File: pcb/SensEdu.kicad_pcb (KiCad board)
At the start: 4 copper layers, 92.7 x 53.4 mm, 139 parts, among them IC1 ADA4511-2ARMZ, IC2 SHT35-DIS-B2.5KS, J1 Analog, J10 Conn_01x04_Pin, J11 Conn_01x04_Pin, J2 Analog, J3 Power, J4 Digital, J5 PWM, J6 PWM, J7 Communication, J8 Conn_01x04_Pin, J9 Conn_01x04_Pin, SW2 NC7SB3157P6X, U1 LM27762DSST, U10 DPS368XTSA1, U2 NCP1117-2.5_SOT223, U3 LT1790ACS6-1.25, U4 AD8426ACPZ-R7, U5 AD8426ACPZ-R7, U6 AD8426ACPZ-R7, U7 AD8426ACPZ-R7, U8 NC7SB3157P6X

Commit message: in works
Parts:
- moved TP_3V3 0.36 mm to (109.0, 66.6)
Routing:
- net +3.3V: track 277.4 -> 267.5 mm, vias 13 -> 14
- net +1.25V_REF: track 80.2 -> 87.9 mm
- net -3V3: track 58.3 -> 59.3 mm
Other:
- board text added: "OP1"
- board text added: "OP2"
- board text added: "OP3"
- board text removed: "AMP1"
- board text removed: "AMP2"
- board text removed: "AMP3"
- board text removed: "AMP4"

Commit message: fix: PCB final fixes
Added simulation for dc offset after ac coupling
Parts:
- removed TP_3V3: TestPoint, TestPoint:TestPoint_THTPad_D2.0mm_Drill1.0mm
- added C52: 1u, Capacitor_SMD:C_0805_2012Metric, F.Cu at (148.0, 67.4)
- added C55: 1u, Capacitor_SMD:C_0805_2012Metric, F.Cu at (156.8, 80.8)
- added TP_TX1: TestPoint, TestPoint:TestPoint_THTPad_D2.0mm_Drill1.0mm, F.Cu at (159.5, 82.3)
- C50, C51: value 2.2u -> 100n
- R30, R31: value 22k -> 1.2k
- moved TP_1V25 0.70 mm to (160.1, 85.9)
- renumbered C52 to C53, C53 to C54, C54 to C56, C55 to C57, C56 to C58, C57 to C59, MIC2 to MK2, MIC3 to MK3, MIC4 to MK4, SW2 to U9
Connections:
- C6 pad 1: +3.3V -> /3V3_INO
- C7 pad 1: +3.3V -> /3V3_INO
- J3 pad 4: /3V3 -> /3V3_INO
- U2 pad 3: +3.3V -> /3V3_INO
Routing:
- net /3V3_INO: track 0.00 -> 77.3 mm
- net +3.3V: track 267.5 -> 246.7 mm
- net /Speakers/+IN_CH1: track 9.82 -> 15.7 mm
- net /+5V_ARDUINO: track 68.0 -> 72.1 mm
- net GND: track 116.6 -> 120.0 mm, vias 86 -> 88
- net +1.25V_REF: track 87.9 -> 85.3 mm
- net -3V3: track 59.3 -> 60.2 mm
- net /OUT_MIC1: track 59.8 -> 60.0 mm, vias 3 -> 5
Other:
- board text removed: "3.3V->1.25V"

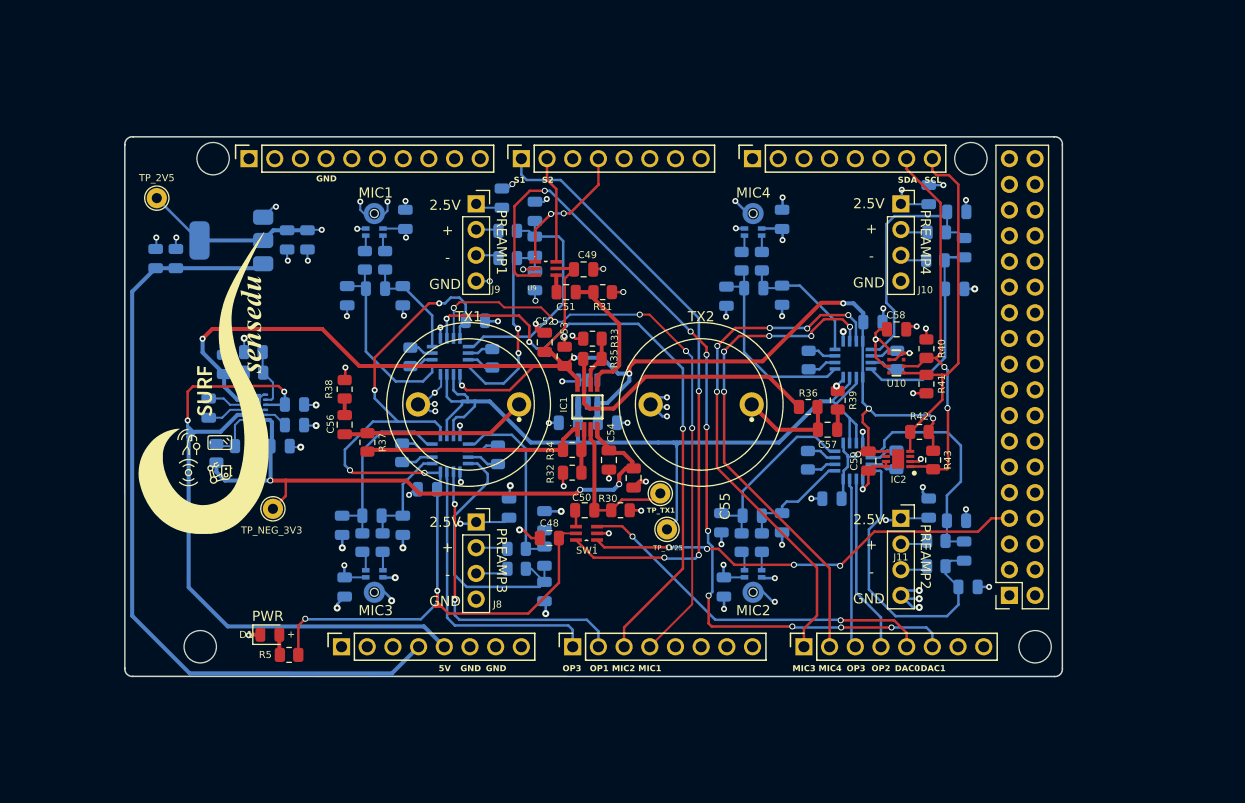
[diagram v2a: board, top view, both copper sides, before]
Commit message: feat: Redraw PCB layout
- Change supply polarity and pin numbers of ADA4511
- Change cap of switches to 100n to reduce bom
- Change supply of sensors to unison 3.3V
- Rearrange mic and amps pins
- Add mountains
- Add Infineon logo
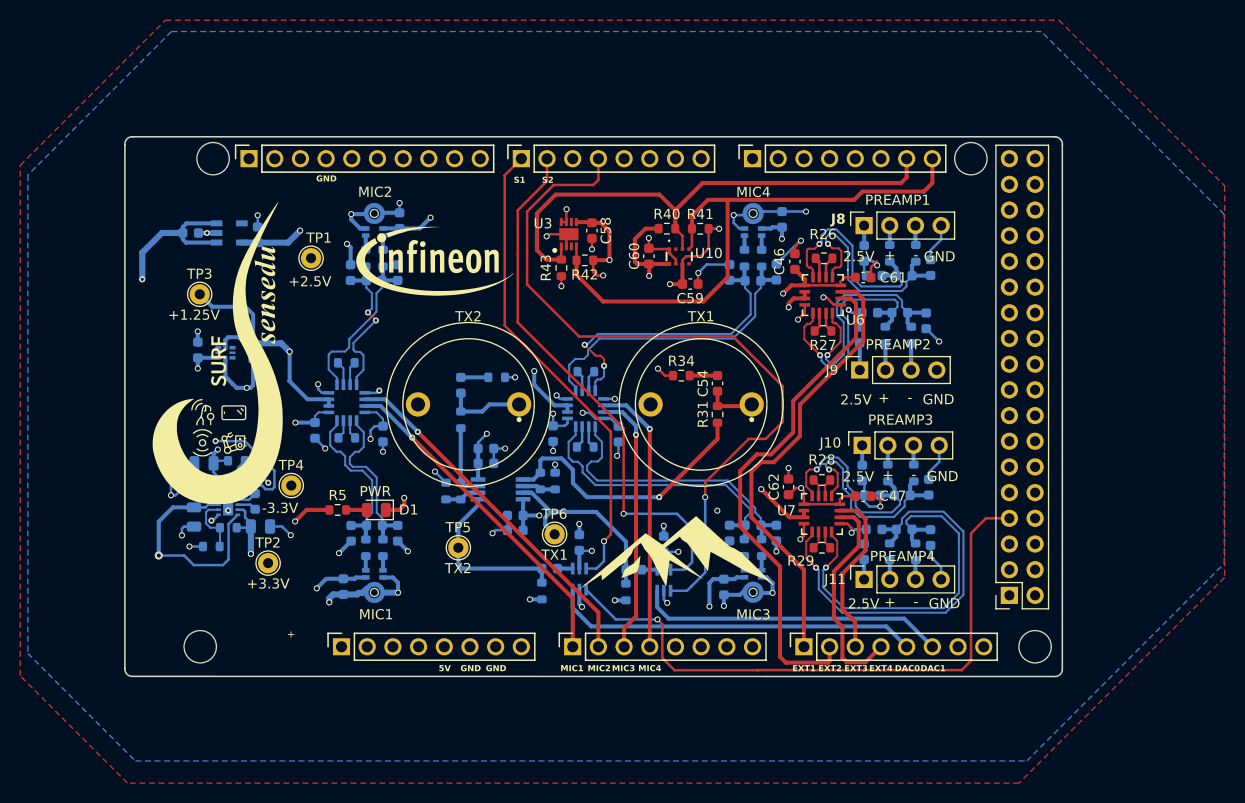
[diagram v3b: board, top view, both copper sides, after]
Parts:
- removed the C34 at (144.5, 83.8)
- removed the C46 at (188.8, 85.0)
- removed the C47 at (186.0, 83.8)
- removed the C6 at (111.6, 59.1)
- removed the C9 at (124.6, 57.2)
- removed IC2: SHT35-DIS-B2.5KS, SensEdu:SHT35-DIS-B2.5KS
- removed the R20 at (145.3, 87.8)
- removed the R26 at (186.7, 59.2)
- removed the R27 at (186.8, 56.5)
- removed the R28 at (186.8, 89.5)
- removed the R29 at (186.8, 87.0)
- removed TP_1V25, TP_2V5, TP_NEG_3V3, TP_TX1: TestPoint, TestPoint:TestPoint_THTPad_D2.0mm_Drill1.0mm
- removed the U2 at (117.0, 57.3)
- added C1: 1u, Capacitor_SMD:C_0603_1608Metric, B.Cu at (132.0, 76.4)
- added C3: 1u, Capacitor_SMD:C_0603_1608Metric, B.Cu at (155.3, 76.4)
- added C35: 470p, Capacitor_SMD:C_0603_1608Metric, B.Cu at (183.6, 85.9)
- added C36: 470p, Capacitor_SMD:C_0603_1608Metric, B.Cu at (183.4, 82.5)
- added C37: 470p, Capacitor_SMD:C_0603_1608Metric, B.Cu at (183.6, 60.8)
- added C59: 100n, Capacitor_SMD:C_0603_1608Metric, F.Cu at (162.4, 61.6)
- added C61: 1u, Capacitor_SMD:C_0603_1608Metric, F.Cu at (179.5, 61.0)
- added C62: 1u, Capacitor_SMD:C_0603_1608Metric, F.Cu at (172.1, 81.7)
- added G***: LOGO, LOGO, F.Cu at (137.4, 59.4)
- added G***: LOGO, LOGO, F.Cu at (161.1, 87.9)
- added R18: 3.9k, Resistor_SMD:R_0603_1608Metric, B.Cu at (184.7, 58.6)
- added R22: 3.9k, Resistor_SMD:R_0603_1608Metric, B.Cu at (184.5, 80.3)
- added R23: 3.9k, Resistor_SMD:R_0603_1608Metric, B.Cu at (182.0, 80.3)
- added R24: 3.9k, Resistor_SMD:R_0603_1608Metric, B.Cu at (184.7, 88.1)
- added R25: 3.9k, Resistor_SMD:R_0603_1608Metric, B.Cu at (182.1, 88.1)
- added TP1: +2.5V, TestPoint:TestPoint_THTPad_D2.0mm_Drill1.0mm, F.Cu at (124.9, 59.0)
- added TP2: +3.3V, TestPoint:TestPoint_THTPad_D2.0mm_Drill1.0mm, F.Cu at (120.7, 89.2)
- added TP3: +1.25V, TestPoint:TestPoint_THTPad_D2.0mm_Drill1.0mm, F.Cu at (113.9, 62.6)
- added TP4: -3.3V, TestPoint:TestPoint_THTPad_D2.0mm_Drill1.0mm, F.Cu at (123.0, 81.5)
- added TP5: TX2, TestPoint:TestPoint_THTPad_D2.0mm_Drill1.0mm, F.Cu at (139.5, 87.7)
- added TP6: TX1, TestPoint:TestPoint_THTPad_D2.0mm_Drill1.0mm, F.Cu at (149.0, 86.3)
- added U1: LDLN025M25R, SamacSys_Parts:SOT95P280X145-5N, B.Cu at (116.8, 56.5)
- added U13: TS3312AQPR, SamacSys_Parts:TS3312AQPR, B.Cu at (116.5, 68.4)
- C10: renamed from C8; value 100n -> 1u; footprint Capacitor_SMD:C_0805_2012Metric -> Capacitor_SMD:C_0603_1608Metric
- C11, C14, C17, C40, C42, C44: footprint Capacitor_SMD:C_0805_2012Metric -> Capacitor_SMD:C_0603_1608Metric
- C12: renamed from C25; footprint Capacitor_SMD:C_0805_2012Metric -> Capacitor_SMD:C_0603_1608Metric
- C13: renamed from C20; footprint Capacitor_SMD:C_0805_2012Metric -> Capacitor_SMD:C_0603_1608Metric
- C15: renamed from C26; footprint Capacitor_SMD:C_0805_2012Metric -> Capacitor_SMD:C_0603_1608Metric
- C16: renamed from C13; footprint Capacitor_SMD:C_0805_2012Metric -> Capacitor_SMD:C_0603_1608Metric
- C18: renamed from C23; footprint Capacitor_SMD:C_0805_2012Metric -> Capacitor_SMD:C_0603_1608Metric
- C19: renamed from C28; footprint Capacitor_SMD:C_0805_2012Metric -> Capacitor_SMD:C_0603_1608Metric
- C2: renamed from C7; value 100n -> 1u; footprint Capacitor_SMD:C_0805_2012Metric -> Capacitor_SMD:C_0603_1608Metric
- C20: renamed from C15; footprint Capacitor_SMD:C_0805_2012Metric -> Capacitor_SMD:C_0603_1608Metric
- C21: renamed from C24; footprint Capacitor_SMD:C_0805_2012Metric -> Capacitor_SMD:C_0603_1608Metric
- C22: renamed from C18; footprint Capacitor_SMD:C_0805_2012Metric -> Capacitor_SMD:C_0603_1608Metric
- C23: renamed from C27; footprint Capacitor_SMD:C_0805_2012Metric -> Capacitor_SMD:C_0603_1608Metric
- C24: renamed from C16; footprint Capacitor_SMD:C_0805_2012Metric -> Capacitor_SMD:C_0603_1608Metric
- C25: renamed from C19; footprint Capacitor_SMD:C_0805_2012Metric -> Capacitor_SMD:C_0603_1608Metric
- C26: renamed from C22; footprint Capacitor_SMD:C_0805_2012Metric -> Capacitor_SMD:C_0603_1608Metric
- C27: renamed from C29; footprint Capacitor_SMD:C_0805_2012Metric -> Capacitor_SMD:C_0603_1608Metric
- C28: renamed from C21; footprint Capacitor_SMD:C_0805_2012Metric -> Capacitor_SMD:C_0603_1608Metric
- C29: renamed from C12; footprint Capacitor_SMD:C_0805_2012Metric -> Capacitor_SMD:C_0603_1608Metric
- C30, C33: value 100p -> 100n; footprint Capacitor_SMD:C_0805_2012Metric -> Capacitor_SMD:C_0603_1608Metric
- C31: renamed from C39; footprint Capacitor_SMD:C_0805_2012Metric -> Capacitor_SMD:C_0603_1608Metric
- C32: value 470p -> 100n; footprint Capacitor_SMD:C_0805_2012Metric -> Capacitor_SMD:C_0603_1608Metric
- C34: renamed from C37; footprint Capacitor_SMD:C_0805_2012Metric -> Capacitor_SMD:C_0603_1608Metric
- C38: renamed from C35; footprint Capacitor_SMD:C_0805_2012Metric -> Capacitor_SMD:C_0603_1608Metric
- C39: renamed from C38; footprint Capacitor_SMD:C_0805_2012Metric -> Capacitor_SMD:C_0603_1608Metric
- C4: renamed from C10; value 100n -> 1u; footprint Capacitor_SMD:C_0805_2012Metric -> Capacitor_SMD:C_0603_1608Metric
- C41, C45: value 470p -> 100p; footprint Capacitor_SMD:C_0805_2012Metric -> Capacitor_SMD:C_0603_1608Metric
- C43: value 100n -> 100p; footprint Capacitor_SMD:C_0805_2012Metric -> Capacitor_SMD:C_0603_1608Metric
- C46: renamed from C31; footprint Capacitor_SMD:C_0805_2012Metric -> Capacitor_SMD:C_0603_1608Metric; moved to F.Cu
- C47: renamed from C36; footprint Capacitor_SMD:C_0805_2012Metric -> Capacitor_SMD:C_0603_1608Metric; moved to F.Cu
- C48: value 10n -> 100n; footprint Capacitor_SMD:C_0805_2012Metric -> Capacitor_SMD:C_0603_1608Metric; moved to B.Cu
- C49: renamed from C52; footprint Capacitor_SMD:C_0805_2012Metric -> Capacitor_SMD:C_0603_1608Metric; moved to B.Cu
- C50: renamed from C53; footprint Capacitor_SMD:C_0805_2012Metric -> Capacitor_SMD:C_0603_1608Metric; moved to B.Cu
- C51: renamed from C54; footprint Capacitor_SMD:C_0805_2012Metric -> Capacitor_SMD:C_0603_1608Metric; moved to B.Cu
- C52: renamed from C55; footprint Capacitor_SMD:C_0805_2012Metric -> Capacitor_SMD:C_0603_1608Metric; moved to B.Cu
- C53: renamed from C50; footprint Capacitor_SMD:C_0805_2012Metric -> Capacitor_SMD:C_0603_1608Metric; moved to B.Cu
- C54: renamed from C56; footprint Capacitor_SMD:C_0805_2012Metric -> Capacitor_SMD:C_0603_1608Metric
- C55: renamed from C57; footprint Capacitor_SMD:C_0805_2012Metric -> Capacitor_SMD:C_0603_1608Metric; moved to B.Cu
- C56: renamed from C49; value 10n -> 100n; footprint Capacitor_SMD:C_0805_2012Metric -> Capacitor_SMD:C_0603_1608Metric; moved to B.Cu
- C57: renamed from C51; footprint Capacitor_SMD:C_0805_2012Metric -> Capacitor_SMD:C_0603_1608Metric; moved to B.Cu
- C58: renamed from C59; footprint Capacitor_SMD:C_0805_2012Metric -> Capacitor_SMD:C_0603_1608Metric
- C60: renamed from C58; footprint Capacitor_SMD:C_0805_2012Metric -> Capacitor_SMD:C_0603_1608Metric
- C8: renamed from C2; footprint Capacitor_SMD:C_0805_2012Metric -> Capacitor_SMD:C_0603_1608Metric
- R1, R17, R19, R2, R3, R4, R42, R43, R5: footprint Resistor_SMD:R_0805_2012Metric -> Resistor_SMD:R_0603_1608Metric
- R10: renamed from R8; footprint Resistor_SMD:R_0805_2012Metric -> Resistor_SMD:R_0603_1608Metric
- R11: renamed from R10; footprint Resistor_SMD:R_0805_2012Metric -> Resistor_SMD:R_0603_1608Metric
- R12: renamed from R13; footprint Resistor_SMD:R_0805_2012Metric -> Resistor_SMD:R_0603_1608Metric
- R13: renamed from R16; footprint Resistor_SMD:R_0805_2012Metric -> Resistor_SMD:R_0603_1608Metric
- R14: renamed from R6; footprint Resistor_SMD:R_0805_2012Metric -> Resistor_SMD:R_0603_1608Metric
- R15: renamed from R11; footprint Resistor_SMD:R_0805_2012Metric -> Resistor_SMD:R_0603_1608Metric
- R16: renamed from R12; footprint Resistor_SMD:R_0805_2012Metric -> Resistor_SMD:R_0603_1608Metric
- R20: renamed from R22; footprint Resistor_SMD:R_0805_2012Metric -> Resistor_SMD:R_0603_1608Metric
- R21: renamed from R24; footprint Resistor_SMD:R_0805_2012Metric -> Resistor_SMD:R_0603_1608Metric
- R26: renamed from R18; footprint Resistor_SMD:R_0805_2012Metric -> Resistor_SMD:R_0603_1608Metric; moved to F.Cu
- R27: renamed from R21; footprint Resistor_SMD:R_0805_2012Metric -> Resistor_SMD:R_0603_1608Metric; moved to F.Cu
- R28: renamed from R23; footprint Resistor_SMD:R_0805_2012Metric -> Resistor_SMD:R_0603_1608Metric; moved to F.Cu
- R29: renamed from R25; footprint Resistor_SMD:R_0805_2012Metric -> Resistor_SMD:R_0603_1608Metric; moved to F.Cu
- R30, R32: footprint Resistor_SMD:R_0805_2012Metric -> Resistor_SMD:R_0603_1608Metric; moved to B.Cu
- R31: renamed from R37; footprint Resistor_SMD:R_0805_2012Metric -> Resistor_SMD:R_0603_1608Metric
- R33: renamed from R34; footprint Resistor_SMD:R_0805_2012Metric -> Resistor_SMD:R_0603_1608Metric; moved to B.Cu
- R34: renamed from R38; footprint Resistor_SMD:R_0805_2012Metric -> Resistor_SMD:R_0603_1608Metric
- R35: renamed from R36; footprint Resistor_SMD:R_0805_2012Metric -> Resistor_SMD:R_0603_1608Metric; moved to B.Cu
- R36: renamed from R33; footprint Resistor_SMD:R_0805_2012Metric -> Resistor_SMD:R_0603_1608Metric; moved to B.Cu
- R37: renamed from R39; footprint Resistor_SMD:R_0805_2012Metric -> Resistor_SMD:R_0603_1608Metric; moved to B.Cu
- R38: renamed from R35; footprint Resistor_SMD:R_0805_2012Metric -> Resistor_SMD:R_0603_1608Metric; moved to B.Cu
- R39: renamed from R31; footprint Resistor_SMD:R_0805_2012Metric -> Resistor_SMD:R_0603_1608Metric; moved to B.Cu
- R40, R41: value 5k6 -> 10k; footprint Resistor_SMD:R_0805_2012Metric -> Resistor_SMD:R_0603_1608Metric
- R6: renamed from R7; footprint Resistor_SMD:R_0805_2012Metric -> Resistor_SMD:R_0603_1608Metric
- R7: renamed from R9; footprint Resistor_SMD:R_0805_2012Metric -> Resistor_SMD:R_0603_1608Metric
- R8: renamed from R14; footprint Resistor_SMD:R_0805_2012Metric -> Resistor_SMD:R_0603_1608Metric
- R9: renamed from R15; footprint Resistor_SMD:R_0805_2012Metric -> Resistor_SMD:R_0603_1608Metric
- U11: renamed from IC1; footprint SensEdu:ADA4511 -> SamacSys_Parts:SOP65P490X110-8N; moved to B.Cu
- U3: value LT1790ACS6-1.25 -> SHT35-DIS-B2.5KS; footprint Package_TO_SOT_SMD:TSOT-23-6 -> SensEdu:SHT35-DIS-B2.5KS; moved to F.Cu
- U6, U7: moved to F.Cu
- U8, U9: moved to B.Cu
- moved R19 48.3 mm to (182.2, 58.6), turned to -90 degrees
- moved J8 48.3 mm to (179.6, 55.8), turned to 90 degrees
- moved C30 46.0 mm to (179.6, 58.6), turned to -90 degrees
- moved R26 45.9 mm to (175.7, 59.0), turned to 180 degrees
- moved C46 42.7 mm to (172.8, 59.4), turned to 90 degrees
- moved R43 41.4 mm to (149.7, 60.0), turned to 90 degrees
- moved J9 41.3 mm to (179.2, 70.1), turned to 90 degrees
- moved C10 41.1 mm to (113.7, 68.1), turned to 90 degrees
- moved R20 40.6 mm to (184.3, 66.6), turned to 90 degrees
- moved U6 40.0 mm to (175.5, 62.7), turned to -90 degrees
- moved C38 38.9 mm to (185.8, 65.2)
- moved R21 38.7 mm to (181.7, 66.6), turned to 90 degrees
- moved C31 37.9 mm to (179.2, 66.6)
- moved R42 37.2 mm to (152.0, 59.2)
- moved C54 37.1 mm to (165.1, 71.4)
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- renumbered C1 to C6, C3 to C7, C4 to C9, J3 to J1, J5 to J2, J1 to J3, J6 to J4, J2 to J5, J7 to J6, J4 to J7, MK3 to MK2, MK2 to MK3, TX2 to TX1, TX1 to TX2, U1 to U2
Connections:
- net /OUT_MIC7 renamed /AMP3_OUT
- net /OUT_MIC8 renamed /AMP4_OUT
- C14 pad 1: mic1_out1 -> mic1_out_P
- C14 pad 2: mic1_out2 -> mic1_out_N
- C15 pad 1: mic3_out1 -> mic2_out_P
- C15 pad 2: mic3_out2 -> mic2_out_N
- C16 pad 2: mic1_out2 -> mic1_out_N
- C17 pad 2: mic1_out1 -> mic1_out_P
- C18 pad 2: mic3_out2 -> mic2_out_N
- C19 pad 2: mic3_out1 -> mic2_out_P
- C22 pad 1: mic2_out1 -> mic3_out_P
- C22 pad 2: mic2_out2 -> mic3_out_N
- C23 pad 1: mic4_out1 -> mic4_out_P
- C23 pad 2: mic4_out2 -> mic4_out_N
- C24 pad 2: mic2_out2 -> mic3_out_N
- C25 pad 2: mic2_out1 -> mic3_out_P
- C26 pad 2: mic4_out2 -> mic4_out_N
- C27 pad 2: mic4_out1 -> mic4_out_P
- C30 pad 1: GND -> +2.5V
- C30 pad 2: mic5_out2 -> GND
- C32 pad 1: mic5_out1 -> +2.5V
- C32 pad 2: mic5_out2 -> GND
- C33 pad 1: GND -> +2.5V
- C33 pad 2: mic5_out1 -> GND
- C34 pad 1: mic6_out1 -> amp2_out_P
- C34 pad 2: mic6_out2 -> amp2_out_N
- C38 pad 2: mic6_out2 -> amp2_out_N
- C39 pad 2: mic6_out1 -> amp2_out_P
- C40 pad 2: mic7_out2 -> amp4_out_N
- C41 pad 1: mic7_out1 -> GND
- C41 pad 2: mic7_out2 -> amp4_out_P
- C42 pad 2: mic7_out1 -> amp3_out_N
- C43 pad 1: +2.5V -> GND
- C43 pad 2: GND -> amp3_out_P
- C44 pad 2: mic8_out2 -> amp1_out_N
- C45 pad 1: mic8_out1 -> GND
- C45 pad 2: mic8_out2 -> amp1_out_P
- C49 pad 1: +3.3V -> -3V3
- C50 pad 1: +3.3V -> -3V3
- C51 pad 2: -3V3 -> +3.3V
- C52 pad 1: -3V3 -> +3.3V
- C60 pad 1: +2.5V -> +3.3V
- J3 pad 1: /OUT_MIC5 -> /MIC1_OUT
- J3 pad 2: /OUT_MIC6 -> /MIC2_OUT
- J3 pad 3: /OUT_MIC2 -> /MIC3_OUT
- J3 pad 4: /OUT_MIC1 -> /MIC4_OUT
- J4 pad 1: S1 -> S2
- J4 pad 2: S2 -> S1
- J5 pad 1: /OUT_MIC3 -> /AMP1_OUT
- J5 pad 2: /OUT_MIC4 -> /AMP2_OUT
- R10 pad 2: mic2_out2 -> mic3_out_N
- R11 pad 2: mic2_out1 -> mic3_out_P
- R12 pad 2: mic4_out2 -> mic4_out_N
- R13 pad 2: mic4_out1 -> mic4_out_P
- R19 pad 1: Net-(J8-Pin_3) -> Net-(J8-Pin_2)
- R19 pad 2: mic5_out2 -> amp1_out_P
- R20 pad 2: mic6_out2 -> amp2_out_N
- R21 pad 2: mic6_out1 -> amp2_out_P
- R40 pad 1: +2.5V -> +3.3V
- R41 pad 2: +2.5V -> +3.3V
- R6 pad 2: mic1_out2 -> mic1_out_N
- R7 pad 2: mic1_out1 -> mic1_out_P
- R8 pad 2: mic3_out2 -> mic2_out_N
- R9 pad 2: mic3_out1 -> mic2_out_P
- TX1 pad 1: /Speakers/TX2 -> /Speakers/TX1
- TX2 pad 1: /Speakers/TX1 -> /Speakers/TX2
- U10 pad 6: +2.5V -> +3.3V
- U10 pad 8: +2.5V -> +3.3V
- U3 pad 1: GND -> /SDA
- U3 pad 4: +3.3V -> /SCL
- U3 pad 5: unconnected-(U3-DNC-Pad5) -> +3.3V
- U3 pad 6: +1.25V_REF -> unconnected-(U3-NRESET-Pad6)
- U4 pad 1: mic6_out1 -> mic1_out_N
- U4 pad 12: mic1_out1 -> mic2_out_N
- U4 pad 14: /OUT_MIC2 -> /MIC2_OUT
- U4 pad 15: /OUT_MIC1 -> /MIC1_OUT
- U4 pad 4: mic6_out2 -> mic1_out_P
- U4 pad 9: mic1_out2 -> mic2_out_P
- U5 pad 1: mic7_out1 -> mic3_out_N
- U5 pad 12: mic4_out1 -> mic4_out_N
- U5 pad 14: /OUT_MIC4 -> /MIC4_OUT
- U5 pad 15: /OUT_MIC3 -> /MIC3_OUT
- U5 pad 4: mic7_out2 -> mic3_out_P
- U5 pad 9: mic4_out2 -> mic4_out_P
- U6 pad 1: mic3_out2 -> amp1_out_N
- U6 pad 12: mic5_out2 -> amp2_out_N
- U6 pad 14: /OUT_MIC6 -> /AMP2_OUT
- U6 pad 15: /OUT_MIC5 -> /AMP1_OUT
- U6 pad 4: mic3_out1 -> amp1_out_P
- U6 pad 9: mic5_out1 -> amp2_out_P
- U7 pad 1: mic2_out2 -> amp3_out_N
- U7 pad 12: mic8_out2 -> amp4_out_N
- U7 pad 4: mic2_out1 -> amp3_out_P
- U7 pad 9: mic8_out1 -> amp4_out_P
- U8 pad 1: SE_PWM_3 -> SE_PWM_1
- U8 pad 3: DAC0 -> DAC1
- U9 pad 1: SE_PWM_1 -> SE_PWM_3
- U9 pad 3: DAC1 -> DAC0
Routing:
- net +3.3V: track 246.7 -> 90.9 mm, vias 14 -> 18
- net /OUT_MIC2: track 60.5 -> 0.00 mm, vias 3 -> 0
- net /OUT_MIC1: track 60.0 -> 0.00 mm, vias 5 -> 0
- net SE_PWM_1: track 13.9 -> 73.8 mm, vias 2 -> 1
- net DAC1: track 86.3 -> 30.5 mm, vias 9 -> 0
- net /OUT_MIC3: track 51.5 -> 0.00 mm, vias 5 -> 0
- net /AMP2_OUT: track 0.00 -> 50.5 mm
- net /OUT_MIC4: track 49.3 -> 0.00 mm, vias 5 -> 0
- net /AMP1_OUT: track 0.00 -> 44.4 mm
- net amp4_out_P: track 0.00 -> 40.2 mm, vias 0 -> 1
- net amp4_out_N: track 0.00 -> 37.6 mm, vias 0 -> 1
- net GND: track 120.0 -> 156.9 mm, vias 88 -> 60
- net S2: track 10.6 -> 47.2 mm, vias 0 -> 1
- net /MIC2_OUT: track 0.00 -> 35.2 mm, vias 0 -> 1
- net /MIC1_OUT: track 0.00 -> 33.2 mm, vias 0 -> 1
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- added copper zone on In2.Cu, net +3.3V
- added copper zone on B.Cu, net GND
- added copper zone on F.Cu, net GND
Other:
- board text added: "."
- board text added: "EXT1"
- board text added: "EXT2"
- board text added: "EXT3"
- board text added: "EXT4"
- board text added: "MK1"
- board text removed: "OP1"
- board text removed: "OP2"
- board text removed: "OP3"
- board text removed: "SCL"
- board text removed: "SDA"

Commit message: feat: Improve PCB design after tests of rev 0.8
- Added new generation of humidity sensor
- New silkscreen information for different components
- Added additional testpoints
- Removed PWM path for ultrasound transmitter
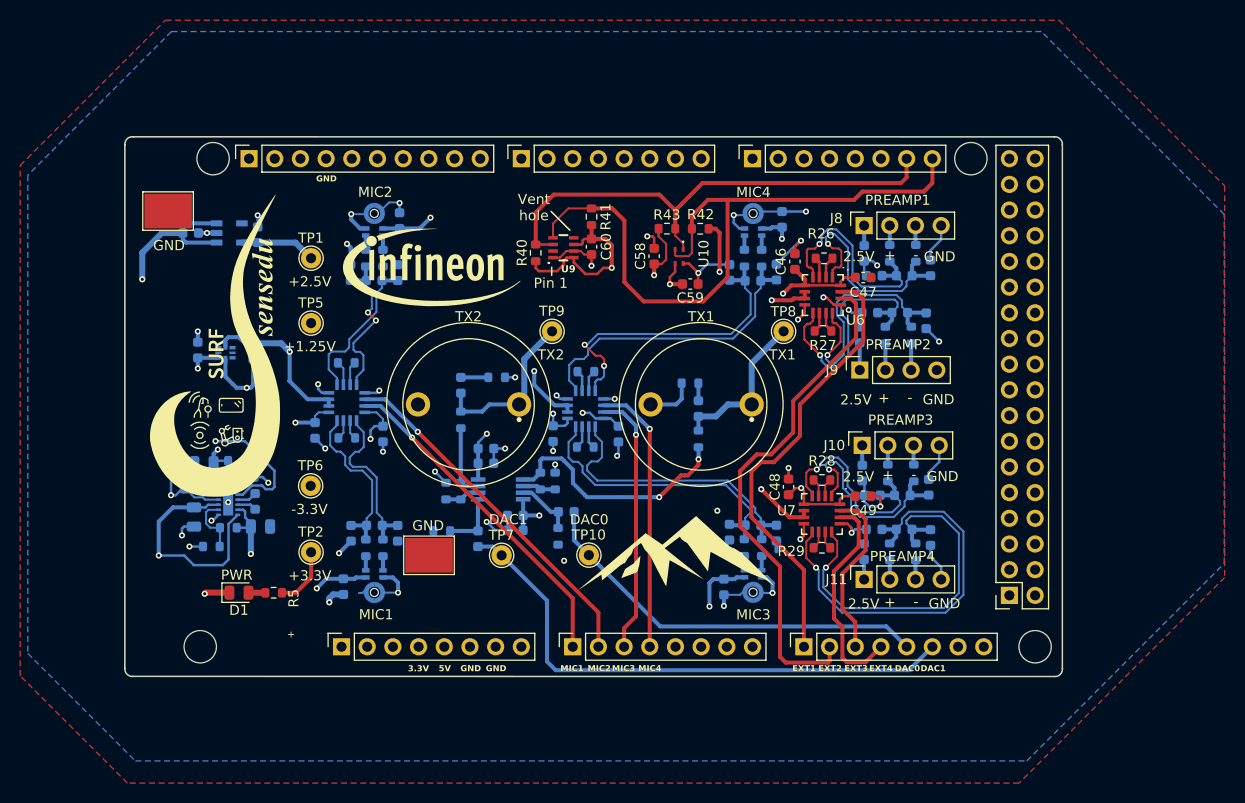
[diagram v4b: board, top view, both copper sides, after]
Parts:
- removed C61, C62: 1u, Capacitor_SMD:C_0603_1608Metric
- removed U11: ADA4511-2ARMZ, SamacSys_Parts:SOP65P490X110-8N
- removed U13: TS3312AQPR, SamacSys_Parts:TS3312AQPR
- added TP10: DAC0, SensEdu:TestPoint_THTPad_D2.0mm_Drill1.0mm, F.Cu at (152.4, 88.4)
- added TP7: DAC1, SensEdu:TestPoint_THTPad_D2.0mm_Drill1.0mm, F.Cu at (143.8, 88.4)
- added TP8: TX1, SensEdu:TestPoint_THTPad_D2.0mm_Drill1.0mm, F.Cu at (171.7, 66.3)
- added TP9: TX2, SensEdu:TestPoint_THTPad_D2.0mm_Drill1.0mm, F.Cu at (148.8, 66.3)
- C1, C16, C17, C2, C24, C25, C28, C29, C30, C31, C32, C33, C34, C35, C36, C37, C38, C39, C40, C41, C42, C43, C44, C45, C46, C47, C53, C55, C58, C59, C60: footprint Capacitor_SMD:C_0603_1608Metric -> SensEdu:C_0603_1608Metric
- C10, C11, C52: value 1u -> 100n; footprint Capacitor_SMD:C_0603_1608Metric -> SensEdu:C_0603_1608Metric
- C12, C13, C20, C21: value 100n -> 470p; footprint Capacitor_SMD:C_0603_1608Metric -> SensEdu:C_0603_1608Metric
- C14, C15, C22, C23: value 470p -> 100p; footprint Capacitor_SMD:C_0603_1608Metric -> SensEdu:C_0603_1608Metric
- C18, C19: value 100p -> 100n; footprint Capacitor_SMD:C_0603_1608Metric -> SensEdu:C_0603_1608Metric
- C26, C27: value 100p -> 1u; footprint Capacitor_SMD:C_0603_1608Metric -> SensEdu:C_0603_1608Metric
- C3, C4: value 1u -> 4.7u; footprint Capacitor_SMD:C_0603_1608Metric -> SensEdu:C_0805_2012Metric
- C48: value 100n -> 1u; footprint Capacitor_SMD:C_0603_1608Metric -> SensEdu:C_0603_1608Metric; moved to F.Cu
- C49: footprint Capacitor_SMD:C_0603_1608Metric -> SensEdu:C_0603_1608Metric; moved to F.Cu
- C5: value 4.7u -> 2.2u; footprint Capacitor_SMD:C_0805_2012Metric -> SensEdu:C_0805_2012Metric
- C50, C57: value 100n -> 1n; footprint Capacitor_SMD:C_0603_1608Metric -> SensEdu:C_0603_1608Metric
- C51: value 100n -> 1u; footprint Capacitor_SMD:C_0603_1608Metric -> SensEdu:C_0603_1608Metric
- C54: value DNI -> 1u; footprint Capacitor_SMD:C_0603_1608Metric -> SensEdu:C_0603_1608Metric; moved to B.Cu
- C56: value 100n -> DNI; footprint Capacitor_SMD:C_0603_1608Metric -> SensEdu:C_0603_1608Metric
- C6: value 4.7u -> 470n; footprint Capacitor_SMD:C_0805_2012Metric -> SensEdu:C_0603_1608Metric
- C7: footprint Capacitor_SMD:C_0805_2012Metric -> SensEdu:C_0805_2012Metric
- C8: value 470n -> 1u; footprint Capacitor_SMD:C_0603_1608Metric -> SensEdu:C_0603_1608Metric
- C9: value 2.2u -> 1u; footprint Capacitor_SMD:C_0805_2012Metric -> SensEdu:C_0603_1608Metric
- D1: footprint LED_SMD:LED_0805_2012Metric -> SensEdu:LED_0805_2012Metric
- G***: footprint LOGO -> SensEdu:LOGO
- J1, J3, J4, J5, J6: footprint Connector_PinSocket_2.54mm:PinSocket_1x08_P2.54mm_Vertical -> SensEdu:PinSocket_1x08_P2.54mm_Vertical
- J10, J11, J8, J9: footprint Connector_PinSocket_2.54mm:PinSocket_1x04_P2.54mm_Vertical -> SensEdu:PinSocket_1x04_P2.54mm_Vertical
- J2: footprint Connector_PinSocket_2.54mm:PinSocket_1x10_P2.54mm_Vertical -> SensEdu:PinSocket_1x10_P2.54mm_Vertical
- J7: footprint Connector_PinSocket_2.54mm:PinSocket_2x18_P2.54mm_Vertical -> SensEdu:PinSocket_2x18_P2.54mm_Vertical
- MH1, MH2, MH5, MH6: footprint Arduino_MountingHole:MountingHole_3.2mm -> SensEdu:MountingHole_3.2mm
- R1, R10, R11, R12, R13, R14, R15, R16, R17, R18, R19, R2, R20, R21, R22, R23, R24, R25, R26, R27, R28, R29, R32, R33, R36, R37, R38, R40, R41, R42, R43, R5, R6, R7, R8, R9: footprint Resistor_SMD:R_0603_1608Metric -> SensEdu:R_0603_1608Metric
- R3: value 130k -> 75k; footprint Resistor_SMD:R_0603_1608Metric -> SensEdu:R_0603_1608Metric
- R30, R39: value 1.2k -> 43k; footprint Resistor_SMD:R_0603_1608Metric -> SensEdu:R_0603_1608Metric
- R31: value 0 -> 100; footprint Resistor_SMD:R_0603_1608Metric -> SensEdu:R_0603_1608Metric; moved to B.Cu
- R34: footprint Resistor_SMD:R_0603_1608Metric -> SensEdu:R_0603_1608Metric; moved to B.Cu
- R35: value 0 -> 100; footprint Resistor_SMD:R_0603_1608Metric -> SensEdu:R_0603_1608Metric
- R4: value 75k -> 130k; footprint Resistor_SMD:R_0603_1608Metric -> SensEdu:R_0603_1608Metric
- TP1, TP2: footprint TestPoint:TestPoint_THTPad_D2.0mm_Drill1.0mm -> SensEdu:TestPoint_THTPad_D2.0mm_Drill1.0mm
- TP3: value +1.25V -> 5018; footprint TestPoint:TestPoint_THTPad_D2.0mm_Drill1.0mm -> SensEdu:5018
- TP4: value -3.3V -> 5018; footprint TestPoint:TestPoint_THTPad_D2.0mm_Drill1.0mm -> SensEdu:5018
- TP5: value TX2 -> +1.25V; footprint TestPoint:TestPoint_THTPad_D2.0mm_Drill1.0mm -> SensEdu:TestPoint_THTPad_D2.0mm_Drill1.0mm
- TP6: value TX1 -> -3.3V; footprint TestPoint:TestPoint_THTPad_D2.0mm_Drill1.0mm -> SensEdu:TestPoint_THTPad_D2.0mm_Drill1.0mm
- U1: footprint SamacSys_Parts:SOT95P280X145-5N -> SensEdu:SOT95P280X145-5N
- U10: value DPS368XTSA1 -> SHT40-AD1F-R2; footprint SensEdu:DPS368XTSA1 -> SensEdu:SHT40AD1FR2
- U3: value SHT35-DIS-B2.5KS -> TS3312AQPR; footprint SensEdu:SHT35-DIS-B2.5KS -> SensEdu:TS3312AQPR; moved to B.Cu
- U8: value NC7SB3157P6X -> ADA4511-2ARMZ; footprint SensEdu:SOT65P210X110-6N -> SensEdu:SOP65P490X110-8N
- U9: value NC7SB3157P6X -> DPS368XTSA1; footprint SensEdu:SOT65P210X110-6N -> SensEdu:DPS368XTSA1; moved to F.Cu
- moved C18 48.3 mm to (165.8, 91.5)
- moved C3 42.3 mm to (113.4, 81.6), turned to 180 degrees
- moved C19 38.4 mm to (171.5, 55.2), turned to 90 degrees
- moved U3 35.9 mm to (116.5, 68.4), turned to 180 degrees
- moved C49 34.5 mm to (179.5, 82.6), turned to 0 degrees
- moved U9 32.8 mm to (149.9, 58.0), turned to 180 degrees
- moved C13 30.4 mm to (131.2, 61.2), turned to 180 degrees
- moved C12 30.2 mm to (131.2, 85.5), turned to 0 degrees
- moved C4 28.6 mm to (113.3, 84.6), turned to -90 degrees
- moved C1 27.5 mm to (113.0, 56.5), turned to 0 degrees
- moved C27 27.3 mm to (148.9, 76.4)
- moved C44 26.7 mm to (186.2, 86.7), turned to 90 degrees
- moved TP5 26.6 mm to (124.9, 65.5)
- moved C25 26.2 mm to (170.9, 60.4), turned to -90 degrees
- moved C16 26.2 mm to (128.8, 60.5), turned to -90 degrees
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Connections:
- net /*10 renamed /CS
- net /*11 renamed /COPI
- net /*12 renamed /CIPO
- net /*13 renamed /SCK
- net /*5 renamed /D5
- net /*8 renamed /SCL2
- net /*9 renamed /SDA2
- net /3* renamed /D2
- net /4* renamed /D3
- C1 pad 1: +3.3V -> /3V3_INO
- C10 pad 1: +3.3V -> +2.5V
- C11 pad 1: GND -> +2.5V
- C11 pad 2: +1.25V_REF -> GND
- C12 pad 1: +2.5V -> mic1_out_P
- C12 pad 2: GND -> mic1_out_N
- C13 pad 1: +2.5V -> mic2_out_P
- C13 pad 2: GND -> mic2_out_N
- C14 pad 1: mic1_out_P -> GND
- C15 pad 1: mic2_out_P -> GND
- C15 pad 2: mic2_out_N -> mic1_out_P
- C16 pad 2: mic1_out_N -> mic2_out_N
- C17 pad 2: mic1_out_P -> mic2_out_P
- C18 pad 1: GND -> +2.5V
- C18 pad 2: mic2_out_N -> GND
- C19 pad 1: GND -> +2.5V
- C19 pad 2: mic2_out_P -> GND
- C2 pad 1: /3V3_INO -> +2.5V
- C20 pad 1: +2.5V -> mic3_out_P
- C20 pad 2: GND -> mic3_out_N
- C21 pad 1: +2.5V -> mic4_out_P
- C21 pad 2: GND -> mic4_out_N
- C22 pad 1: mic3_out_P -> GND
- C23 pad 1: mic4_out_P -> GND
- C23 pad 2: mic4_out_N -> mic3_out_P
- C24 pad 2: mic3_out_N -> mic4_out_N
- C25 pad 2: mic3_out_P -> mic4_out_P
- C26 pad 1: GND -> +3.3V
- C26 pad 2: mic4_out_N -> GND
- C27 pad 1: GND -> +3.3V
- C27 pad 2: mic4_out_P -> GND
- C3 pad 1: +3.3V -> /Power/CP
- C34 pad 1: amp2_out_P -> amp1_out_P
- C34 pad 2: amp2_out_N -> amp1_out_N
- C35 pad 1: amp4_out_P -> amp2_out_P
- C35 pad 2: amp4_out_N -> amp2_out_N
- C37 pad 1: amp1_out_P -> amp4_out_P
- C37 pad 2: amp1_out_N -> amp4_out_N
- C38 pad 2: amp2_out_N -> amp1_out_N
- C39 pad 2: amp2_out_P -> amp1_out_P
- C4 pad 1: +2.5V -> /+5V_ARDUINO
- C40 pad 2: amp4_out_N -> amp2_out_N
- C41 pad 2: amp4_out_P -> amp2_out_P
- C44 pad 2: amp1_out_N -> amp4_out_N
- C45 pad 2: amp1_out_P -> amp4_out_P
- C48 pad 1: GND -> +3.3V
- C48 pad 2: +3.3V -> GND
- C49 pad 1: -3V3 -> +3.3V
- C5 pad 1: /Power/CP -> +3.3V
- C50 pad 1: -3V3 -> DAC1
- C50 pad 2: GND -> /Speakers/+IN_CH2
- C51 pad 1: GND -> -3V3
- C51 pad 2: +3.3V -> GND
- C52 pad 1: +3.3V -> -3V3
- C53 pad 1: /Speakers/SW1_OUT -> GND
- C53 pad 2: /Speakers/+IN_CH1 -> +3.3V
- C54 pad 1: /Speakers/TX1 -> +3.3V
- C54 pad 2: Net-(C54-Pad2) -> GND
- C55 pad 1: /Speakers/TX2 -> /Speakers/TX1
- C56 pad 1: GND -> /Speakers/TX2
- C56 pad 2: +3.3V -> Net-(C56-Pad2)
- C57 pad 1: /Speakers/SW2_OUT -> DAC0
- C57 pad 2: /Speakers/+IN_CH2 -> /Speakers/+IN_CH1
- C6 pad 1: /+5V_ARDUINO -> Net-(U2-C1+)
- C6 pad 2: GND -> Net-(U2-C1-)
- C7 pad 1: +3.3V -> GND
- C7 pad 2: GND -> -3V3
- C8 pad 1: Net-(U2-C1+) -> +3.3V
- C8 pad 2: Net-(U2-C1-) -> GND
- C9 pad 2: -3V3 -> +1.25V_REF
- J3 pad 6: unconnected-(J3-Pin_6-Pad6) -> /A5
- J3 pad 7: unconnected-(J3-Pin_7-Pad7) -> /A6
- J3 pad 8: unconnected-(J3-Pin_8-Pad8) -> /A7
- J4 pad 1: S2 -> /D7
- J4 pad 2: S1 -> /D6
- J4 pad 4: SE_PWM_1 -> /D4
- J7 pad 20: SE_PWM_2 -> unconnected-(J7-Pin_20-Pad20)
- J7 pad 7: SE_PWM_3 -> unconnected-(J7-Pin_7-Pad7)
- R30 pad 2: /Speakers/+IN_CH1 -> /Speakers/+IN_CH2
- R34 pad 2: Net-(C54-Pad2) -> Net-(C55-Pad2)
- R37 pad 2: Net-(C55-Pad2) -> Net-(C56-Pad2)
- R39 pad 2: /Speakers/+IN_CH2 -> /Speakers/+IN_CH1
- TP3 pad 1: +1.25V_REF -> GND
- TP4 pad 1: -3V3 -> GND
- TP5 pad 1: /Speakers/+IN_CH2 -> +1.25V_REF
- TP6 pad 1: /Speakers/+IN_CH1 -> -3V3
- U10 pad 1: GND -> /SDA
- U10 pad 2: unconnected-(U10-~{CSB}-Pad2) -> /SCL
- U10 pad 3: /SDA -> +3.3V
- U10 pad 4: /SCL -> GND
- U3 pad 1: /SDA -> unconnected-(U3-NC_1-Pad1)
- U3 pad 2: GND -> unconnected-(U3-NC_2-Pad2)
- U3 pad 4: /SCL -> GND
- U3 pad 7: GND -> unconnected-(U3-NC_5-Pad7)
- U3 pad 8: GND -> +1.25V_REF
- U8 pad 1: SE_PWM_1 -> /Speakers/TX1_IN
- U8 pad 2: GND -> /Speakers/-IN_CH1
- U8 pad 3: DAC1 -> /Speakers/+IN_CH1
- U8 pad 4: /Speakers/SW1_OUT -> -3V3
- U8 pad 5: +3.3V -> /Speakers/+IN_CH2
- U8 pad 6: S1 -> /Speakers/-IN_CH2
- U9 pad 1: SE_PWM_3 -> GND
- U9 pad 2: GND -> unconnected-(U9-~{CSB}-Pad2)
- U9 pad 3: DAC0 -> /SDA
- U9 pad 4: /Speakers/SW2_OUT -> /SCL
- U9 pad 5: +3.3V -> unconnected-(U9-SDO-Pad5)
- U9 pad 6: S2 -> +3.3V
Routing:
- net SE_PWM_1: track 73.8 -> 0.00 mm, vias 1 -> 0
- net SE_PWM_3: track 60.7 -> 0.00 mm, vias 1 -> 0
- net S1: track 53.8 -> 0.00 mm, vias 1 -> 0
- net S2: track 47.2 -> 0.00 mm, vias 1 -> 0
- net DAC1: track 30.5 -> 54.5 mm
- net /Speakers/+IN_CH1: track 19.2 -> 5.88 mm
- net GND: track 156.9 -> 144.6 mm, vias 60 -> 49
- net /Speakers/+IN_CH2: track 17.1 -> 5.89 mm
- net /Speakers/TX1: track 4.92 -> 15.7 mm
- net /SCL: track 58.5 -> 69.0 mm
- net /Speakers/TX2: track 7.88 -> 16.5 mm
- net +1.25V_REF: track 106.2 -> 102.1 mm
- net DAC0: track 36.4 -> 40.1 mm
- net /SDA: track 53.1 -> 50.3 mm
- net /Speakers/TX1_IN: track 27.1 -> 24.3 mm, vias 1 -> 2
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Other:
- board text added: "3.3V"
- board text added: "3.3V -> 1.25V"
- board text added: "Pin 1"
- board text added: "Vent hole"
- board text removed: "S1"
- board text removed: "S2"
